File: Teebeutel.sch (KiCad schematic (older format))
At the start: 162 parts, among them J1 RJ45_Shielded, J2 Battery, J3 Micro_SD_Card, J4 Conn_01x30_Female, J5 Conn_01x10_Female, J6 Conn_01x10_Female, M1 Motor_DC, Q1 S8050, Q2 S8050, Q3 BSN20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

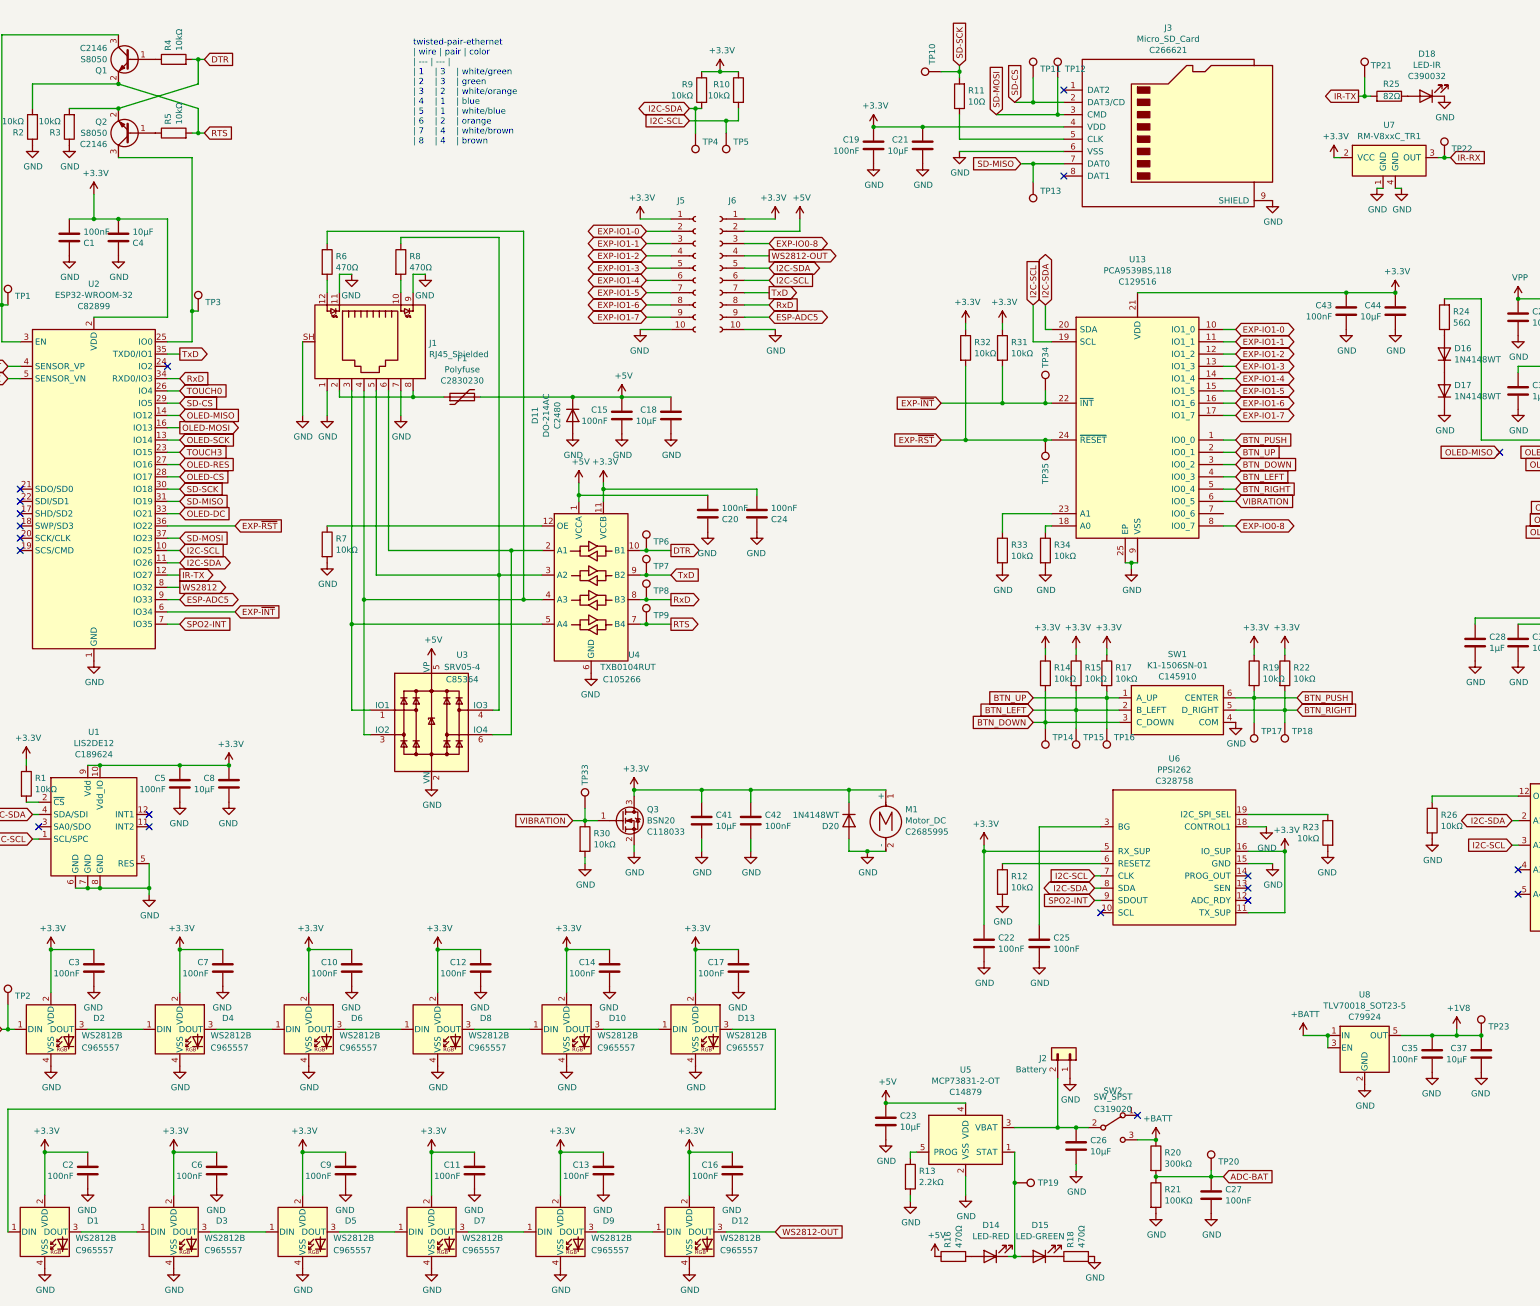
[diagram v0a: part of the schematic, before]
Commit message: Add vibration motor
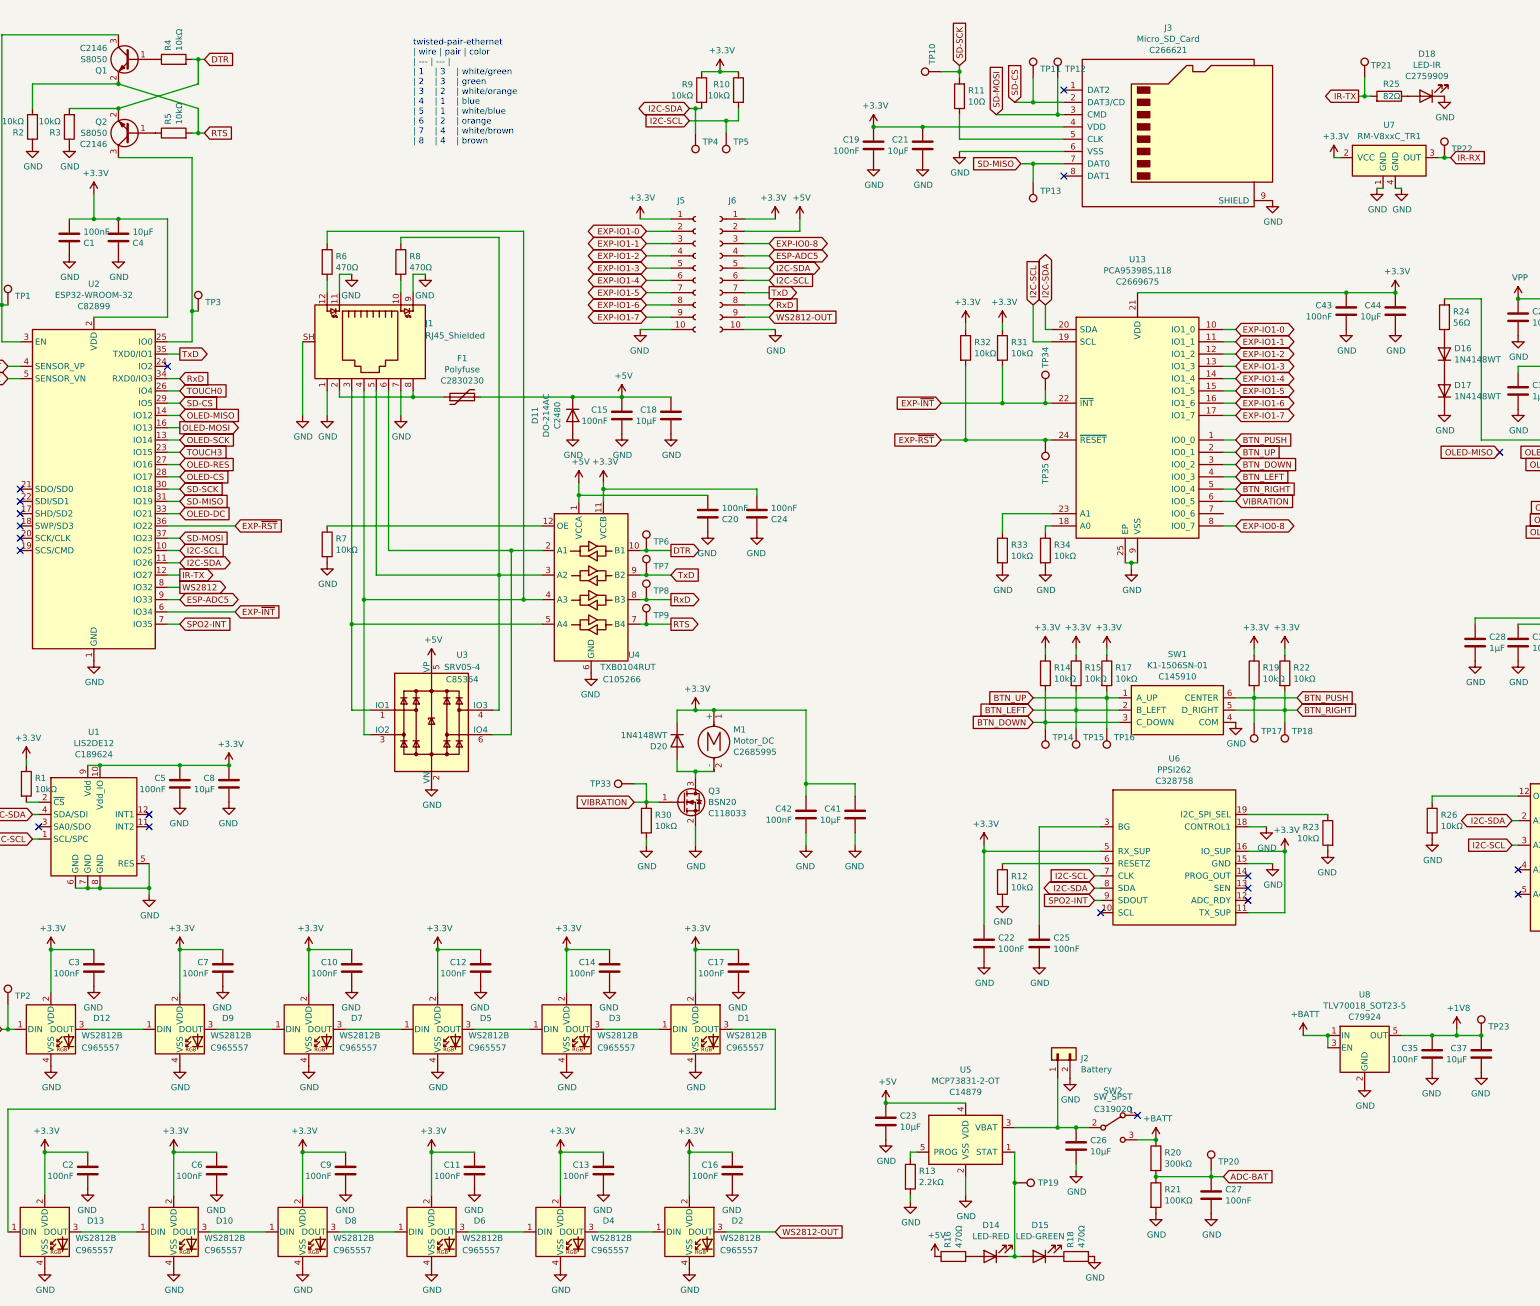
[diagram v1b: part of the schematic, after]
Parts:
- D18: LCSC C390032 -> C2759909
- J2: footprint Connector_PinHeader_2.54mm:PinHeader_1x02_P2.54mm_Vertical -> Connector_Molex:Molex_PicoBlade_53261-0271_1x02-1MP_P1.25mm_Horizontal
- J5: footprint Connector_PinHeader_1.00mm:PinHeader_1x10_P1.00mm_Vertical_SMD_Pin1Left -> Connector_PinSocket_2.54mm:PinSocket_1x10_P2.54mm_Vertical_SMD_Pin1Left
- J6: footprint Connector_PinHeader_1.00mm:PinHeader_1x10_P1.00mm_Vertical_SMD_Pin1Right -> Connector_PinSocket_2.54mm:PinSocket_1x10_P2.54mm_Vertical_SMD_Pin1Right
- M1: footprint (none) -> Teebeutel_Special_Parts:LNLON-S3070P
- U13: LCSC C129516 -> C2669675
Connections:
- net +3V3: no longer Q3.3 (D)
- net ESP-ADC5: now also J6.4 (Pin_4); no longer J6.9 (Pin_9)
- net GND: now also J2.2 (Pin_2); no longer D20.2 (A), J2.1 (Pin_1), M1.2 (-)
- net WS2812: now also D12.1 (DIN); no longer D2.1 (DIN)
- net WS2812-OUT: now also D2.3 (DOUT), J6.9 (Pin_9); no longer D12.3 (DOUT), J6.4 (Pin_4)
- net at D4.1 (DIN): now also D6.3 (DOUT); no longer D2.3 (DOUT)
- net at D4.3 (DOUT): now also D2.1 (DIN); no longer D6.1 (DIN)
- net at D8.1 (DIN): now also D10.3 (DOUT); no longer D6.3 (DOUT)
- net at D8.3 (DOUT): now also D6.1 (DIN); no longer D10.1 (DIN)
- net at C26.1, SW2.2 (B), U5.3 (VBAT): now also J2.1 (Pin_1); no longer J2.2 (Pin_2)
- net at D9.1 (DIN): now also D12.3 (DOUT); no longer D7.3 (DOUT)
- net at D9.3 (DOUT): now also D7.1 (DIN); no longer D12.1 (DIN)
- net at D13.1 (DIN): now also D1.3 (DOUT); no longer D10.3 (DOUT)
- net at D13.3 (DOUT): now also D10.1 (DIN); no longer D1.1 (DIN)
- net at D5.1 (DIN): now also D7.3 (DOUT); no longer D3.3 (DOUT)
- net at D5.3 (DOUT): now also D3.1 (DIN); no longer D7.1 (DIN)
- new net: D1.1 (DIN), D3.3 (DOUT)
- new net: D20.2 (A), M1.2 (-), Q3.3 (D)
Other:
- moved on the sheet: C41, C42, D1, D10, D12, D13, D2, D20, D3, D4, D5, D6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

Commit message: feat: more routing work
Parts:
- Q3: value BSN20 -> AO3400; LCSC C118033 -> C841146
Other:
- moved on the sheet: J5, J6
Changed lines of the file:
@@
 Wire Wire Line
 	7000 10500 7400 10500
-Text GLabel 7350 3050 2    50   Input ~ 0
+Text GLabel 6250 3100 0    50   Input ~ 0
 WS2812-OUT
-Text GLabel 7350 2650 2    50   BiDi ~ 0
+Text GLabel 6250 2700 0    50   BiDi ~ 0
 I2C-SDA
-Text GLabel 7350 2750 2    50   Input ~ 0
+Text GLabel 6250 2800 0    50   Input ~ 0
 I2C-SCL
 $Comp
 L power:GND #PWR0143
 U 1 1 629B5C38
-P 7400 3150
-F 0 "#PWR0143" H 7400 2900 50  0001 C CNN
-F 1 "GND" H 7405 2977 50  0000 C CNN
-F 2 "" H 7400 3150 50  0001 C CNN
-F 3 "" H 7400 3150 50  0001 C CNN
-	1    7400 3150
-	1    0    0    -1
+P 6200 3200
+F 0 "#PWR0143" H 6200 2950 50  0001 C CNN
+F 1 "GND" H 6205 3027 50  0000 C CNN
+F 2 "" H 6200 3200 50  0001 C CNN
+F 3 "" H 6200 3200 50  0001 C CNN
+	1    6200 3200
+	-1   0    0    -1
 $EndComp
 $Comp
 L power:+3.3V #PWR0144
 U 1 1 629EAE39
-P 6300 2250
-F 0 "#PWR0144" H 6300 2100 50  0001 C CNN
-F 1 "+3.3V" H 6315 2423 50  0000 C CNN
-F 2 "" H 6300 2250 50  0001 C CNN
-F 3 "" H 6300 2250 50  0001 C CNN
-	1    6300 2250
-	1    0    0    -1
-$EndComp
-Text GLabel 7350 2950 2    50   Input ~ 0
+P 7200 2300
+F 0 "#PWR0144" H 7200 2150 50  0001 C CNN
+F 1 "+3.3V" H 7215 2473 50  0000 C CNN
+F 2 "" H 7200 2300 50  0001 C CNN
+F 3 "" H 7200 2300 50  0001 C CNN
+	1    7200 2300
+	-1   0    0    -1
+$EndComp
+Text GLabel 6250 3000 0    50   Input ~ 0
 RxD
-Text GLabel 7350 2850 2    50   Output ~ 0
+Text GLabel 6250 2900 0    50   Output ~ 0
 TxD
 $Comp
@@
 P 6650 7000
 F 0 "Q3" H 6854 7091 50  0000 L CNN
-F 1 "BSN20" H 6854 7000 50  0000 L CNN
+F 1 "AO3400" H 6854 7000 50  0000 L CNN
 F 2 "Package_TO_SOT_SMD:SOT-23" H 6850 6925 50  0001 L CIN
 F 3 "http://www.diodes.com/assets/Datasheets/ds31898.pdf" H 6650 7000 50  0001 L CNN
-F 4 " C118033" H 6854 6909 50  0000 L CNN "LCSC"
+F 4 "C841146" H 6854 6909 50  0000 L CNN "LCSC"
 	1    6650 7000
 	1    0    0    -1
@@
 Wire Wire Line
 	2550 5350 2450 5350
-Text GLabel 7350 2550 2    50   BiDi ~ 0
+Text GLabel 6250 2600 0    50   BiDi ~ 0
 ESP-ADC5
 $Comp
@@
 $EndComp
 Wire Wire Line
-	6350 2350 6550 2350
-Wire Wire Line
-	6550 2450 6350 2450
-Wire Wire Line
-	6350 2550 6550 2550
-Wire Wire Line
-	6550 2650 6350 2650
-Wire Wire Line
-	6350 2750 6550 2750
-Wire Wire Line
-	6350 2850 6550 2850
-Wire Wire Line
-	6550 2950 6350 2950
-Wire Wire Line
-	6350 3050 6550 3050
+	7150 2400 6950 2400
+Wire Wire Line
+	6950 2500 7150 2500
+Wire Wire Line
+	7150 2600 6950 2600
+Wire Wire Line
+	6950 2700 7150 2700
+Wire Wire Line
+	7150 2800 6950 2800
+Wire Wire Line
+	7150 2900 6950 2900
+Wire Wire Line
+	6950 3000 7150 3000
+Wire Wire Line
+	7150 3100 6950 3100
 $Comp
 L Connector:Conn_01x10_Female J6
 U 1 1 6553A1D9
-P 6950 2650
-F 0 "J6" H 6850 3200 50  0000 C CNN
-F 1 "Conn_01x10_Female" H 6842 3144 50  0001 C CNN
-F 2 "Connector_PinSocket_2.54mm:PinSocket_1x10_P2.54mm_Vertical_SMD_Pin1Right" H 6950 2650 50  0001 C CNN
-F 3 "~" H 6950 2650 50  0001 C CNN
-	1    6950 2650
-	-1   0    0    -1
-$EndComp
-Wire Wire Line
-	7150 2450 7350 2450
-Wire Wire Line
-	7350 2550 7150 2550
-Wire Wire Line
-	7150 2650 7350 2650
-Wire Wire Line
-	7350 2750 7150 2750
-Wire Wire Line
-	7150 2850 7350 2850
-Wire Wire Line
-	7150 2950 7350 2950
-Wire Wire Line
-	7350 3050 7150 3050
-Wire Wire Line
-	6300 2250 6550 2250
+P 6650 2700
+F 0 "J6" H 6550 3250 50  0000 C CNN
+F 1 "Conn_01x10_Female" H 6542 3194 50  0001 C CNN
+F 2 "Connector_PinSocket_2.54mm:PinSocket_1x10_P2.54mm_Vertical_SMD_Pin1Right" H 6650 2700 50  0001 C CNN
+F 3 "~" H 6650 2700 50  0001 C CNN
+	1    6650 2700
+	1    0    0    -1
+$EndComp
+Wire Wire Line
+	6450 2500 6250 2500
+Wire Wire Line
+	6250 2600 6450 2600
+Wire Wire Line
+	6450 2700 6250 2700
+Wire Wire Line
+	6250 2800 6450 2800
+Wire Wire Line
+	6450 2900 6250 2900
+Wire Wire Line
+	6450 3000 6250 3000
+Wire Wire Line
+	6250 3100 6450 3100
+Wire Wire Line
+	7200 2300 6950 2300
 $Comp
 L power:+3.3V #PWR0154
 U 1 1 6578F5C7
-P 7400 2250
-F 0 "#PWR0154" H 7400 2100 50  0001 C CNN
-F 1 "+3.3V" H 7415 2423 50  0000 C CNN
-F 2 "" H 7400 2250 50  0001 C CNN
-F 3 "" H 7400 2250 50  0001 C CNN
-	1    7400 2250
-	-1   0    0    -1
-$EndComp
-Wire Wire Line
-	7400 2250 7150 2250
-Wire Wire Line
-	7150 3150 7400 3150
+P 6200 2300
+F 0 "#PWR0154" H 6200 2150 50  0001 C CNN
+F 1 "+3.3V" H 6215 2473 50  0000 C CNN
+F 2 "" H 6200 2300 50  0001 C CNN
+F 3 "" H 6200 2300 50  0001 C CNN
+	1    6200 2300
+	1    0    0    -1
+$EndComp
+Wire Wire Line
+	6200 2300 6450 2300
+Wire Wire Line
+	6450 3200 6200 3200
 $Comp
 L power:GND #PWR0151
 U 1 1 6589BE45
-P 6300 3150
-F 0 "#PWR0151" H 6300 2900 50  0001 C CNN
-F 1 "GND" H 6305 2977 50  0000 C CNN
-F 2 "" H 6300 3150 50  0001 C CNN
-F 3 "" H 6300 3150 50  0001 C CNN
-	1    6300 3150
-	-1   0    0    -1
-$EndComp
-Wire Wire Line
-	6550 3150 6300 3150
+P 7200 3200
+F 0 "#PWR0151" H 7200 2950 50  0001 C CNN
+F 1 "GND" H 7205 3027 50  0000 C CNN
+F 2 "" H 7200 3200 50  0001 C CNN
+F 3 "" H 7200 3200 50  0001 C CNN
+	1    7200 3200
+	1    0    0    -1
+$EndComp
+Wire Wire Line
+	6950 3200 7200 3200
 $Comp
 L power:+5V #PWR0155
 U 1 1 65920A95
-P 7600 2250
-F 0 "#PWR0155" H 7600 2100 50  0001 C CNN
-F 1 "+5V" H 7615 2423 50  0000 C CNN
-F 2 "" H 7600 2250 50  0001 C CNN
-F 3 "" H 7600 2250 50  0001 C CNN
-	1    7600 2250
-	1    0    0    -1
-$EndComp
-Wire Wire Line
-	7150 2350 7600 2350
-Wire Wire Line
-	7600 2350 7600 2250
+P 6000 2300
+F 0 "#PWR0155" H 6000 2150 50  0001 C CNN
+F 1 "+5V" H 6015 2473 50  0000 C CNN
+F 2 "" H 6000 2300 50  0001 C CNN
+F 3 "" H 6000 2300 50  0001 C CNN
+	1    6000 2300
+	-1   0    0    -1
+$EndComp
+Wire Wire Line
+	6450 2400 6000 2400
+Wire Wire Line
+	6000 2400 6000 2300
 Wire Wire Line
 	8500 9850 8500 9900
@@
 Text GLabel 2550 5550 2    50   Input ~ 0
 SPO2-INT
-Text GLabel 6350 3050 0    50   BiDi ~ 0
+Text GLabel 7150 3100 2    50   BiDi ~ 0
 EXP-IO1-7
-Text GLabel 6350 2950 0    50   BiDi ~ 0
+Text GLabel 7150 3000 2    50   BiDi ~ 0
 EXP-IO1-6
-Text GLabel 6350 2850 0    50   BiDi ~ 0
+Text GLabel 7150 2900 2    50   BiDi ~ 0
 EXP-IO1-5
-Text GLabel 6350 2750 0    50   BiDi ~ 0
+Text GLabel 7150 2800 2    50   BiDi ~ 0
 EXP-IO1-4
-Text GLabel 6350 2650 0    50   BiDi ~ 0
+Text GLabel 7150 2700 2    50   BiDi ~ 0
 EXP-IO1-3
-Text GLabel 6350 2550 0    50   BiDi ~ 0
+Text GLabel 7150 2600 2    50   BiDi ~ 0
 EXP-IO1-2
-Text GLabel 6350 2450 0    50   BiDi ~ 0
+Text GLabel 7150 2500 2    50   BiDi ~ 0
 EXP-IO1-1
-Text GLabel 6350 2350 0    50   BiDi ~ 0
+Text GLabel 7150 2400 2    50   BiDi ~ 0
 EXP-IO1-0
 Text GLabel 11150 3850 2    50   BiDi ~ 0
@@
 Wire Wire Line
 	14400 4400 14400 4500
-Text GLabel 7350 2450 2    50   BiDi ~ 0
+Text GLabel 6250 2500 0    50   BiDi ~ 0
 EXP-IO0-8
 Text GLabel 11150 4750 2    50   BiDi ~ 0
@@
 L Connector:Conn_01x10_Female J5
 U 1 1 65472ECD
-P 6750 2650
-F 0 "J5" H 6600 3200 50  0000 L CNN
-F 1 "Conn_01x10_Female" H 6778 2535 50  0001 L CNN
-F 2 "Connector_PinSocket_2.54mm:PinSocket_1x10_P2.54mm_Vertical_SMD_Pin1Left" H 6750 2650 50  0001 C CNN
-F 3 "~" H 6750 2650 50  0001 C CNN
-	1    6750 2650
-	1    0    0    -1
-$EndComp
-Wire Wire Line
+P 6750 2700
+F 0 "J5" H 6600 3250 50  0000 L CNN
+F 1 "Conn_01x10_Female" H 6778 2585 50  0001 L CNN
+F 2 "Connector_PinSocket_2.54mm:PinSocket_1x10_P2.54mm_Vertical_SMD_Pin1Left" H 6750 2700 50  0001 C CNN
+F 3 "~" H 6750 2700 50  0001 C CNN
+	1    6750 2700
+	-1   0    0    -1
+$EndComp
+Wire Wire Line

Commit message: feat: add I²C Addresses
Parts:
- added R35: 10kΩ, Resistor_SMD:R_0603_1608Metric, symbol Device:R
- U1: I²C (none) -> 0x32
- U12: I²C (none) -> 0x58
- U13: I²C (none) -> 0x74
- U6: I²C (none) -> 0x5B
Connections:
- net GND: now also R35.2
- net at U6.13 (SEN): now also R35.1
- no-connect marks 28 -> 27
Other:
- moved on the sheet: TP1
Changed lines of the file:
@@
 F 4 "C189624" H 1850 7789 50  0000 C CNN "LCSC"
 F 5 "LGA-12_2.0x2.0x0.5P" H 1800 7200 50  0001 C CNN "JLC"
+F 6 "0x32" H 2100 7050 50  0000 C CNN "I²C"
 	1    1800 7200
 	1    0    0    -1
@@
 F 4 "C514454" H 15000 7033 50  0000 C CNN "LCSC"
 F 5 "DFN-6_EP_2.5x2.5x0.8P" H 15000 7000 50  0001 C CNN "JLC"
+F 6 "0x58" H 15100 6700 50  0000 C CNN "I²C"
 	1    15000 7000
 	1    0    0    -1
@@
 	2700 1550 2750 1550
 Wire Wire Line
-	1100 3250 1100 2950
+	1100 3250 1100 3000
 Wire Wire Line
 	1100 750  2050 750
@@
 NoConn ~ 11250 7600
 NoConn ~ 11250 7800
-NoConn ~ 11250 7700
 $Comp
 L Teebeutel_Special_Parts:PPSI262 U6
@@
 F 4 "C328758" H 10650 6873 50  0000 C CNN "LCSC"
 F 5 "SENSOR-SMD" H 10650 6850 50  0001 C CNN "JLC"
+F 6 "0x5B" H 10650 6250 50  0000 C CNN "I²C"
 	1    10650 6850
 	1    0    0    -1
@@
 L Connector:TestPoint TP1
 U 1 1 61930C43
-P 1150 2950
-F 0 "TP1" H 1208 3022 50  0000 L CNN
-F 1 "ESP32 EN" H 1208 2977 50  0001 L CNN
-F 2 "TestPoint:TestPoint_Pad_D1.0mm" H 1350 2950 50  0001 C CNN
-F 3 "~" H 1350 2950 50  0001 C CNN
-	1    1150 2950
+P 1150 3000
+F 0 "TP1" H 1208 3072 50  0000 L CNN
+F 1 "ESP32 EN" H 1208 3027 50  0001 L CNN
+F 2 "TestPoint:TestPoint_Pad_D1.0mm" H 1350 3000 50  0001 C CNN
+F 3 "~" H 1350 3000 50  0001 C CNN
+	1    1150 3000
 	1    0    0    -1
 $EndComp
@@
 	0    1    1    0
 $EndComp
-Wire Wire Line
-	1150 2950 1100 2950
 $Comp
 L Device:C C3
@@
 	2650 1750 2650 3000
 Connection ~ 2650 3000
-Wire Wire Line
-	1100 750  1100 2950
-Connection ~ 1100 2950
+Connection ~ 1100 3000
 $Comp
 L power:GND #PWR08
@@
 F 3 "http://www.nxp.com/docs/en/data-sheet/PCA9539_PCA9539R.pdf" H 11400 4350 50  0001 L CNN
 F 4 "C2669675" H 10350 5139 50  0000 C CNN "LCSC"
+F 5 "0x74" H 10350 3950 50  0000 C CNN "I²C"
 	1    10350 3950
 	1    0    0    -1
@@
 	1    0    0    -1
 $EndComp
+Wire Wire Line
+	1150 3000 1100 3000
+Wire Wire Line
+	1100 750  1100 3000
+$Comp
+L Device:R R35
+U 1 1 61BB1574
+P 11900 7850
+F 0 "R35" H 11970 7896 50  0000 L CNN
+F 1 "10kΩ" H 11970 7805 50  0000 L CNN
+F 2 "Resistor_SMD:R_0603_1608Metric" V 11830 7850 50  0001 C CNN
+F 3 "~" H 11900 7850 50  0001 C CNN
+F 4 "0603" H 11900 7850 50  0001 C CNN "JLC"
+F 5 "C25804" H 11900 7850 50  0001 C CNN "LCSC"
+	1    11900 7850
+	-1   0    0    -1
+$EndComp
+Wire Wire Line
+	11900 7700 11250 7700
+$Comp
+L power:GND #PWR0115
+U 1 1 61BB157B
+P 11900 8000
+F 0 "#PWR0115" H 11900 7750 50  0001 C CNN
+F 1 "GND" H 11905 7827 50  0000 C CNN
+F 2 "" H 11900 8000 50  0001 C CNN
+F 3 "" H 11900 8000 50  0001 C CNN
+	1    11900 8000
+	-1   0    0    -1
+$EndComp
 $EndSCHEMATC
